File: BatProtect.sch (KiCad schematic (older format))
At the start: 57 parts, among them J1 PC104, J13 Charge3+, J16 uInv2+, J17 uInv1+, J19 uInv3+, J2 VBat1+, J3 BCharge1+, J4 BCharge3+, J5 Charge1+, J7 BCharge2+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

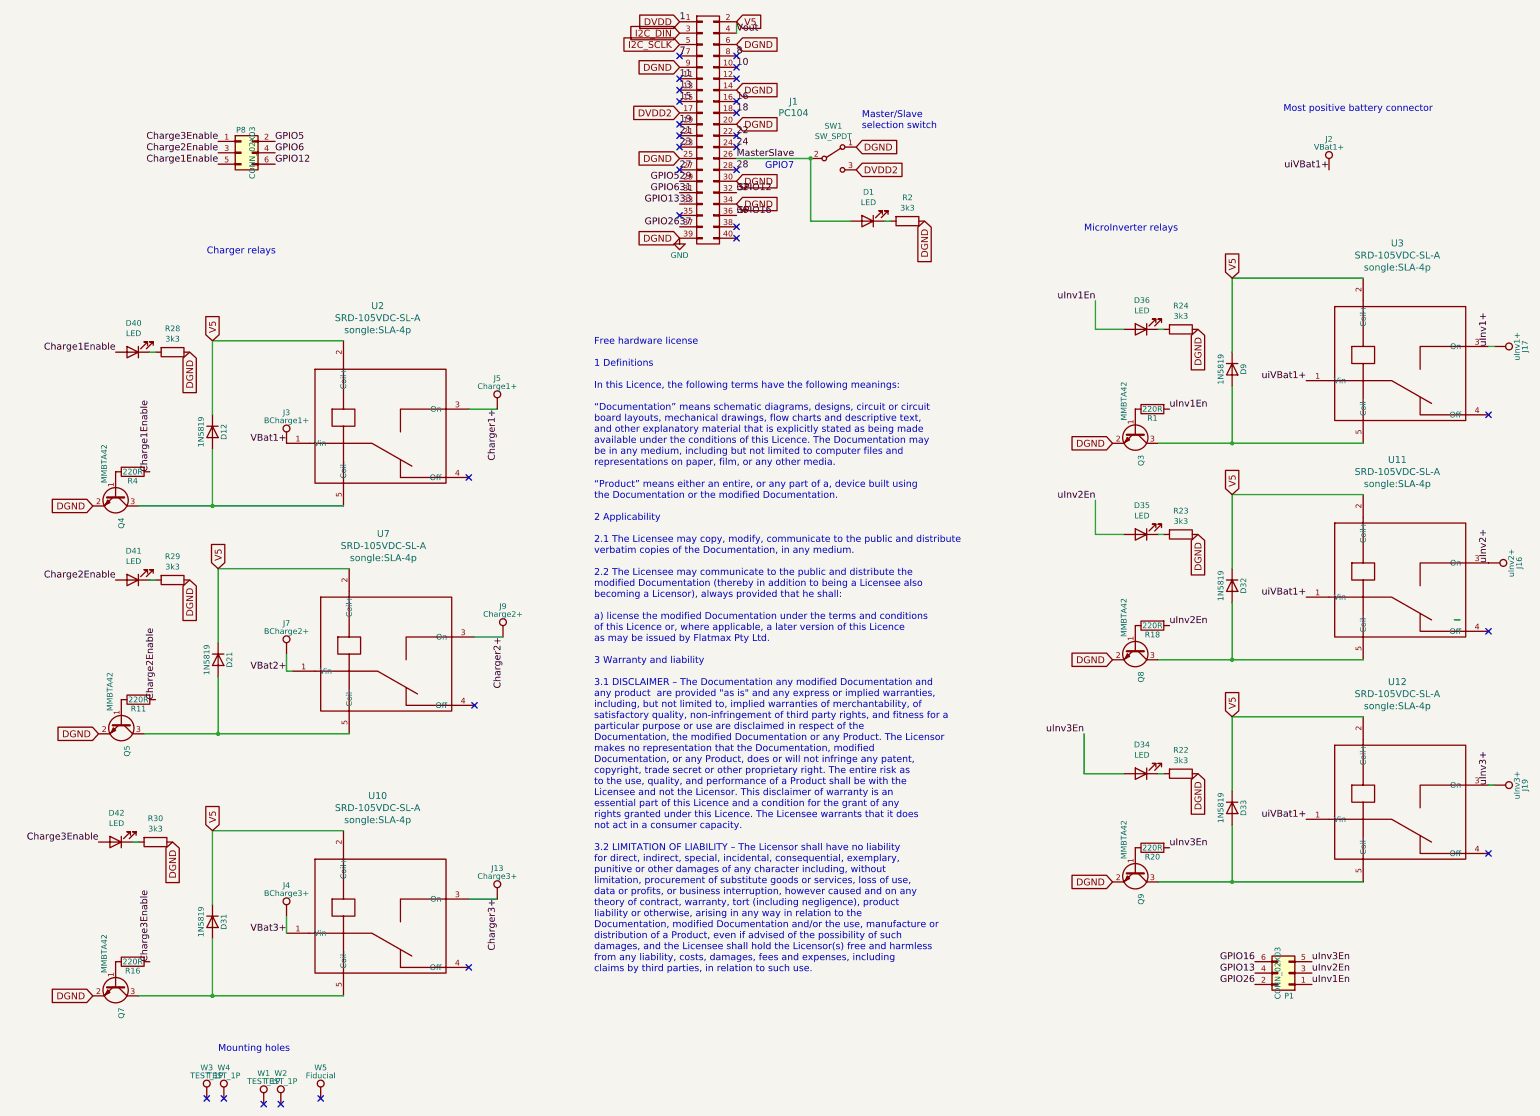
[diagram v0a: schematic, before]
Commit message: v2.0 Changed to AC mains relay switching.
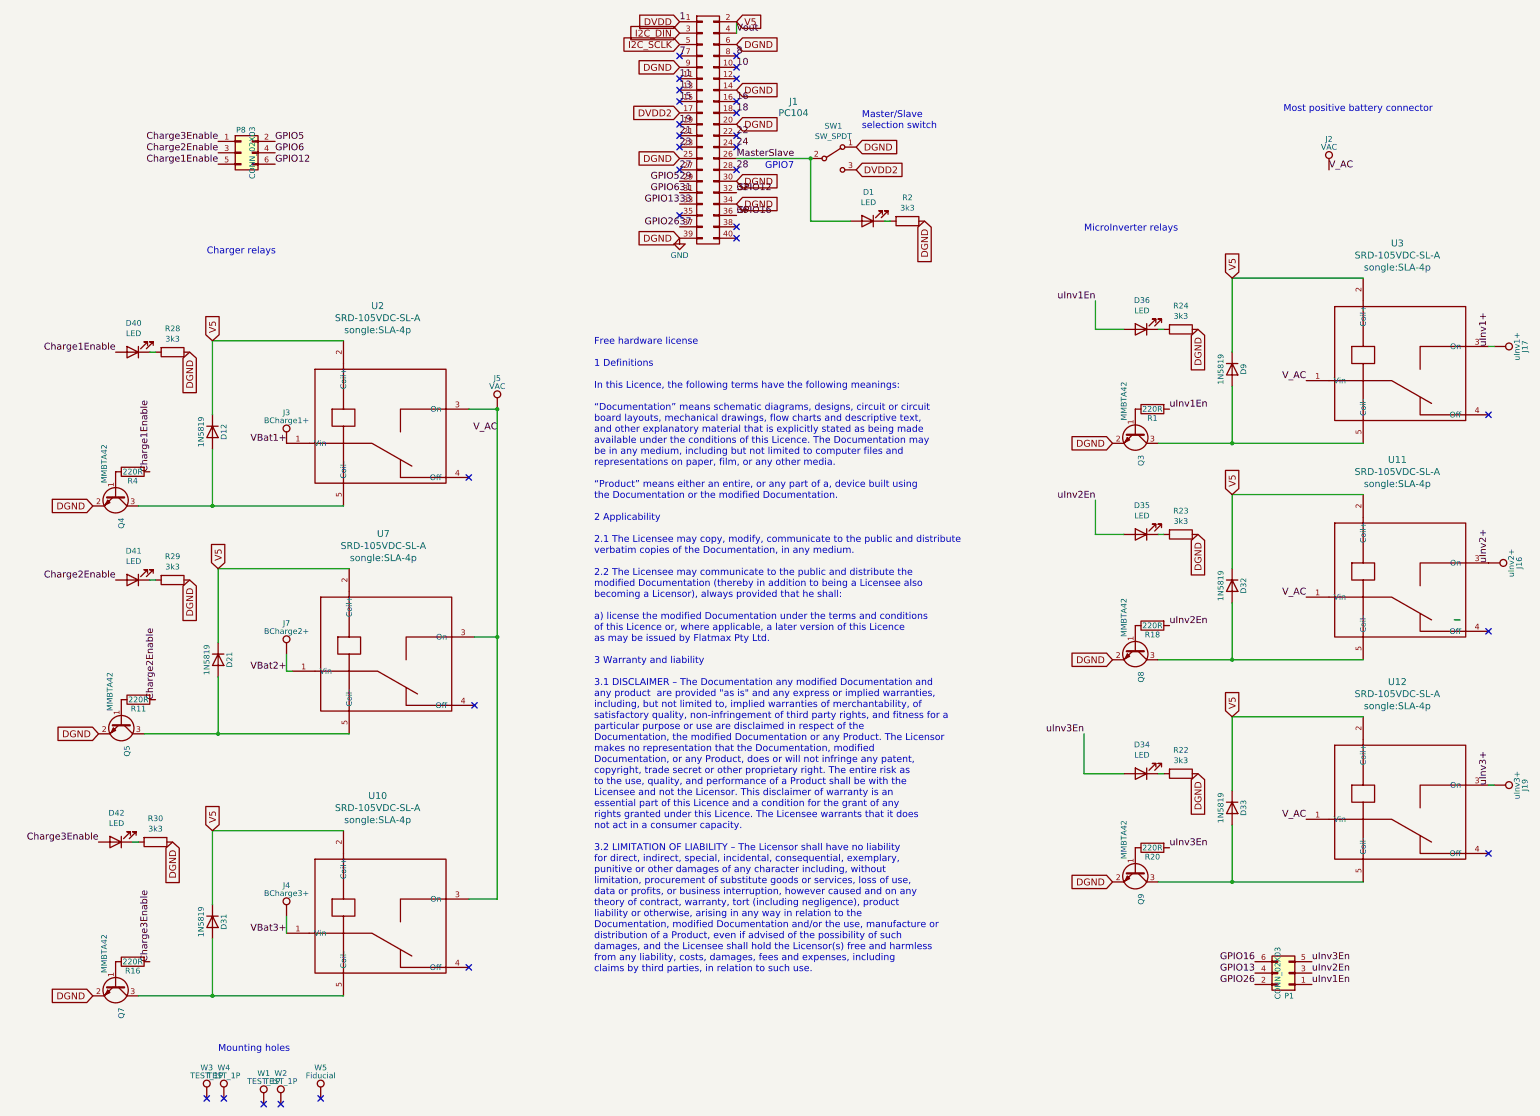
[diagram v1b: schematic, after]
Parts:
- removed J13: Charge3+, holes:Pin4mm, symbol BatProtect-rescue:TEST_1P
- removed J9: Charge2+, holes:Pin4mm, symbol BatProtect-rescue:TEST_1P
- J2: value VBat1+ -> VAC
- J5: value Charge1+ -> VAC
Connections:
- net labels added: V_AC
- net labels removed: Charger1+, Charger2+, Charger3+, uiVBat1+
- wire segments 56 -> 58
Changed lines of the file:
@@
 EESchema Schematic File Version 4
-LIBS:BatProtect-cache
 EELAYER 30 0
 EELAYER END
@@
 P 5850 4500
 F 0 "J5" H 5850 4770 50  0000 C CNN
-F 1 "Charge1+" H 5850 4700 50  0000 C CNN
+F 1 "VAC" H 5850 4700 50  0000 C CNN
 F 2 "holes:Pin4mm" H 6050 4500 50  0001 C CNN
 F 3 "" H 6050 4500 50  0000 C CNN
@@
 Text Label 2800 5050 1    60   ~ 0
 Charge1Enable
-Text Label 5850 4500 3    60   ~ 0
-Charger1+
 NoConn ~ 5600 5100
 $Comp
@@
 	1    0    0    -1
 $EndComp
-$Comp
-L BatProtect-rescue:TEST_1P J9
-U 1 1 5D644226
-P 5900 6500
-F 0 "J9" H 5900 6770 50  0000 C CNN
-F 1 "Charge2+" H 5900 6700 50  0000 C CNN
-F 2 "holes:Pin4mm" H 6100 6500 50  0001 C CNN
-F 3 "" H 6100 6500 50  0000 C CNN
-	1    5900 6500
-	1    0    0    -1
-$EndComp
 Text Label 2850 7050 1    60   ~ 0
 Charge2Enable
-Text Label 5900 6500 3    60   ~ 0
-Charger2+
 NoConn ~ 5650 7100
 $Comp
@@
 DGND
 Connection ~ 3400 7350
-Wire Wire Line
-	5650 6500 5900 6500
 $Comp
 L srd-12vdc-sl-c:SRD-12VDC-SL-C U7
@@
 	1    0    0    -1
 $EndComp
-$Comp
-L BatProtect-rescue:TEST_1P J13
-U 1 1 5D6503F2
-P 5850 8800
-F 0 "J13" H 5850 9070 50  0000 C CNN
-F 1 "Charge3+" H 5850 9000 50  0000 C CNN
-F 2 "holes:Pin4mm" H 6050 8800 50  0001 C CNN
-F 3 "" H 6050 8800 50  0000 C CNN
-	1    5850 8800
-	1    0    0    -1
-$EndComp
 Text Label 2800 9350 1    60   ~ 0
 Charge3Enable
-Text Label 5850 8800 3    60   ~ 0
-Charger3+
 NoConn ~ 5600 9400
 $Comp
@@
 P 13150 2400
 F 0 "J2" H 13150 2670 50  0000 C CNN
-F 1 "VBat1+" H 13150 2600 50  0000 C CNN
+F 1 "VAC" H 13150 2600 50  0000 C CNN
 F 2 "holes:Pin4mm" H 13350 2400 50  0001 C CNN
 F 3 "" H 13350 2400 50  0000 C CNN
@@
 	1    0    0    -1
 $EndComp
-Text Label 12950 4250 2    60   ~ 0
-uiVBat1+
 $Comp
 L BatProtect-rescue:TEST_1P J7
@@
 	1    0    0    -1
 $EndComp
-Text Label 12950 6150 2    60   ~ 0
-uiVBat1+
-Text Label 12950 8100 2    60   ~ 0
-uiVBat1+
 NoConn ~ 4300 10550
 Text Label 4000 4800 2    60   ~ 0
@@
 Text Label 4000 9100 2    60   ~ 0
 VBat3+
-Text Label 13150 2400 2    60   ~ 0
-uiVBat1+
 $Comp
 L BatProtect-rescue:TEST_1P J3
@@
 Text Notes 6700 9450 0    60   ~ 0
 Free hardware license\n\n1 Definitions\n\nIn this Licence, the following terms have the following meanings:\n\n“Documentation” means schematic diagrams, designs, circuit or circuit\nboard layouts, mechanical drawings, flow charts and descriptive text,\nand other explanatory material that is explicitly stated as being made\navailable under the conditions of this Licence. The Documentation may\nbe in any medium, including but not limited to computer files and\nrepresentations on paper, film, or any other media.\n\n“Product” means either an entire, or any part of a, device built using\nthe Documentation or the modified Documentation.\n\n2 Applicability\n\n2.1 The Licensee may copy, modify, communicate to the public and distribute\nverbatim copies of the Documentation, in any medium.\n\n2.2 The Licensee may communicate to the public and distribute the\nmodified Documentation (thereby in addition to being a Licensee also\nbecoming a Licensor), always provided that he shall:\n\na) license the modified Documentation under the terms and conditions\nof this Licence or, where applicable, a later version of this Licence\nas may be issued by Flatmax Pty Ltd.\n\n3 Warranty and liability\n\n3.1 DISCLAIMER – The Documentation any modified Documentation and\nany product  are provided "as is" and any express or implied warranties,\nincluding, but not limited to, implied warranties of merchantability, of\nsatisfactory quality, non-infringement of third party rights, and fitness for a\nparticular purpose or use are disclaimed in respect of the\nDocumentation, the modified Documentation or any Product. The Licensor\nmakes no representation that the Documentation, modified\nDocumentation, or any Product, does or will not infringe any patent,\ncopyright, trade secret or other proprietary right. The entire risk as\nto the use, quality, and performance of a Product shall be with the\nLicensee and not the Licensor. This disclaimer of warranty is an\nessential part of this Licence and a condition for the grant of any\nrights granted under this Licence. The Licensee warrants that it does\nnot act in a consumer capacity.\n\n3.2 LIMITATION OF LIABILITY – The Licensor shall have no liability\nfor direct, indirect, special, incidental, consequential, exemplary,\npunitive or other damages of any character including, without\nlimitation, procurement of substitute goods or services, loss of use,\ndata or profits, or business interruption, however caused and on any\ntheory of contract, warranty, tort (including negligence), product\nliability or otherwise, arising in any way in relation to the\nDocumentation, modified Documentation and/or the use, manufacture or\ndistribution of a Product, even if advised of the possibility of such\ndamages, and the Licensee shall hold the Licensor(s) free and harmless\nfrom any liability, costs, damages, fees and expenses, including\nclaims by third parties, in relation to such use.\n
+Wire Wire Line
+	5850 4500 5850 6500
+Connection ~ 5850 4500
+Wire Wire Line
+	5650 6500 5850 6500
+Connection ~ 5850 6500
+Wire Wire Line
+	5850 6500 5850 8800
+Text Label 13150 2400 0    60   ~ 0
+V_AC
+Text Label 12950 4250 2    60   ~ 0
+V_AC
+Text Label 12950 6150 2    60   ~ 0
+V_AC
+Text Label 12950 8100 2    60   ~ 0
+V_AC
+Text Label 5850 4700 2    60   ~ 0
+V_AC
 $EndSCHEMATC

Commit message: Switched relay names.
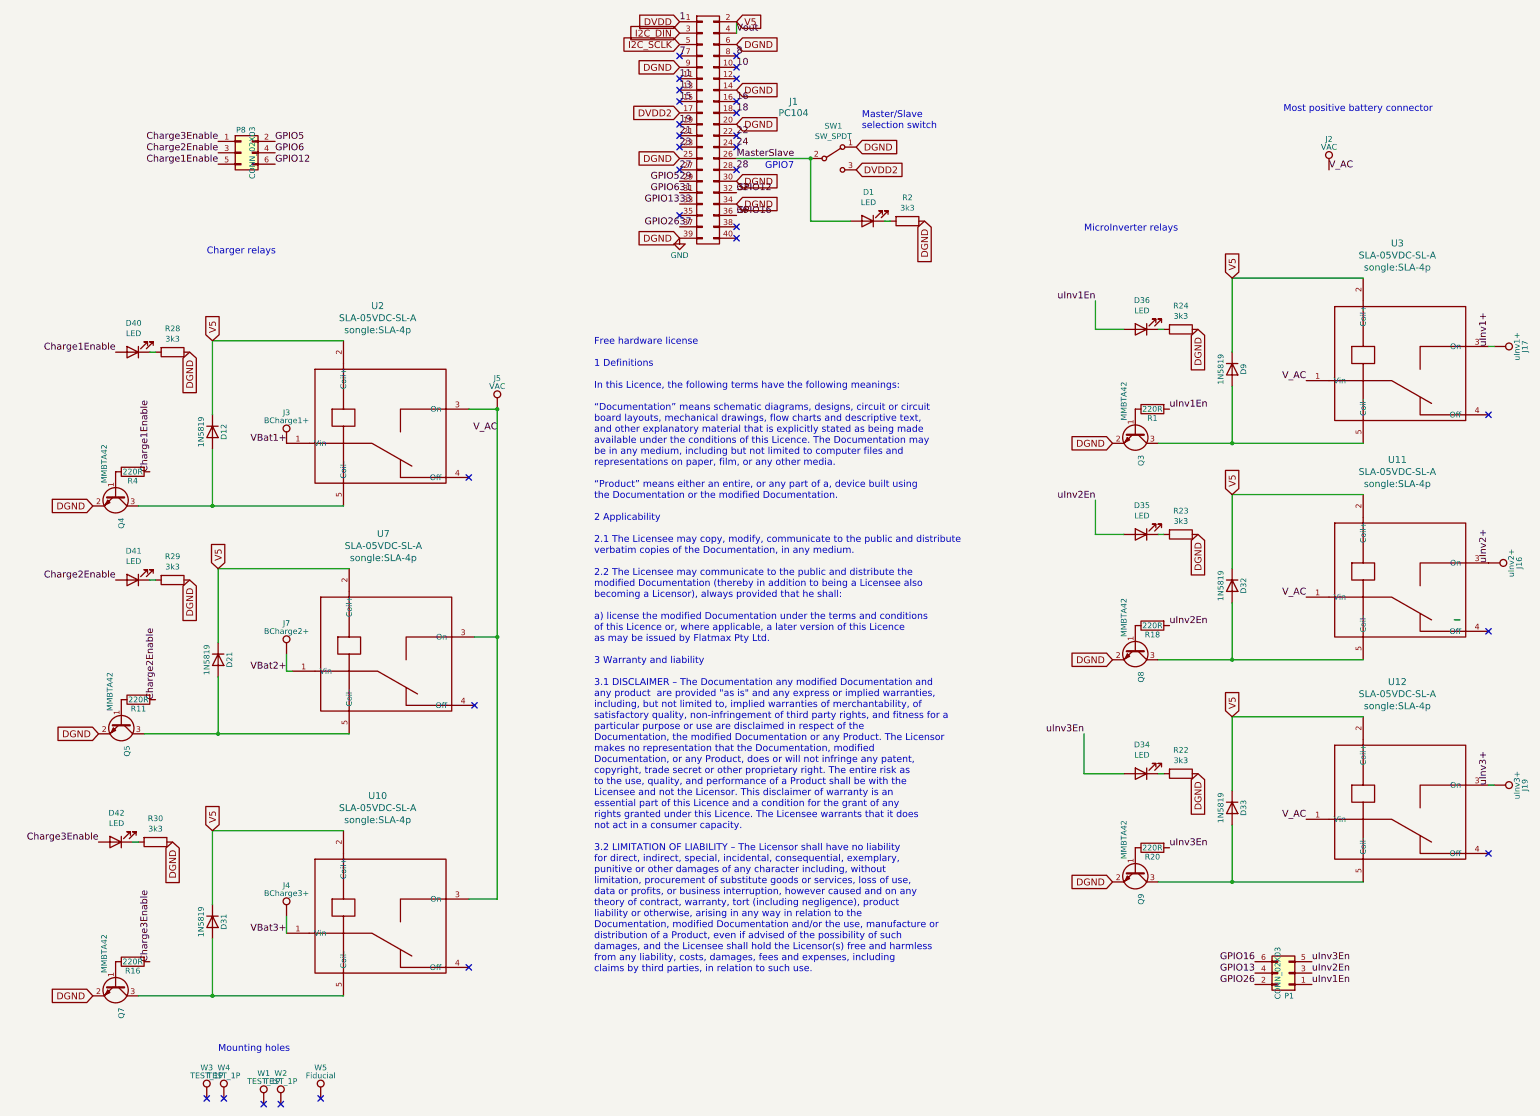
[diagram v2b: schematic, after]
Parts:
- U10, U11, U12, U2, U3, U7: value SRD-105VDC-SL-A -> SLA-05VDC-SL-A
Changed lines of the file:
@@
 Text Label 14550 3950 1    60   ~ 0
 uInv1+
-$Comp
-L srd-12vdc-sl-c:SRD-12VDC-SL-C U3
-U 1 1 5D6292DF
-P 13850 4250
-F 0 "U3" H 13750 5456 60  0000 C CNN
-F 1 "SRD-105VDC-SL-A" H 13750 5350 60  0000 C CNN
-F 2 "songle:SLA-4p" H 13750 5244 60  0000 C CNN
-F 3 "" H 13850 4250 60  0000 C CNN
-	1    13850 4250
-	1    0    0    -1
-$EndComp
 NoConn ~ 14550 4550
 $Comp
@@
 P 4900 4800
 F 0 "U2" H 4800 6006 60  0000 C CNN
-F 1 "SRD-105VDC-SL-A" H 4800 5900 60  0000 C CNN
+F 1 "SLA-05VDC-SL-A" H 4800 5900 60  0000 C CNN
 F 2 "songle:SLA-4p" H 4800 5794 60  0000 C CNN
 F 3 "" H 4900 4800 60  0000 C CNN
@@
 P 4950 6800
 F 0 "U7" H 4850 8006 60  0000 C CNN
-F 1 "SRD-105VDC-SL-A" H 4850 7900 60  0000 C CNN
+F 1 "SLA-05VDC-SL-A" H 4850 7900 60  0000 C CNN
 F 2 "songle:SLA-4p" H 4850 7794 60  0000 C CNN
 F 3 "" H 4950 6800 60  0000 C CNN
@@
 P 4900 9100
 F 0 "U10" H 4800 10306 60  0000 C CNN
-F 1 "SRD-105VDC-SL-A" H 4800 10200 60  0000 C CNN
+F 1 "SLA-05VDC-SL-A" H 4800 10200 60  0000 C CNN
 F 2 "songle:SLA-4p" H 4800 10094 60  0000 C CNN
 F 3 "" H 4900 9100 60  0000 C CNN
@@
 P 13850 6150
 F 0 "U11" H 13750 7356 60  0000 C CNN
-F 1 "SRD-105VDC-SL-A" H 13750 7250 60  0000 C CNN
+F 1 "SLA-05VDC-SL-A" H 13750 7250 60  0000 C CNN
 F 2 "songle:SLA-4p" H 13750 7144 60  0000 C CNN
 F 3 "" H 13850 6150 60  0000 C CNN
@@
 P 13850 8100
 F 0 "U12" H 13750 9306 60  0000 C CNN
-F 1 "SRD-105VDC-SL-A" H 13750 9200 60  0000 C CNN
+F 1 "SLA-05VDC-SL-A" H 13750 9200 60  0000 C CNN
 F 2 "songle:SLA-4p" H 13750 9094 60  0000 C CNN
 F 3 "" H 13850 8100 60  0000 C CNN
@@
 Text Label 5850 4700 2    60   ~ 0
 V_AC
+$Comp
+L srd-12vdc-sl-c:SRD-12VDC-SL-C U3
+U 1 1 5D6292DF
+P 13850 4250
+F 0 "U3" H 13750 5456 60  0000 C CNN
+F 1 "SLA-05VDC-SL-A" H 13750 5350 60  0000 C CNN
+F 2 "songle:SLA-4p" H 13750 5244 60  0000 C CNN
+F 3 "" H 13850 4250 60  0000 C CNN
+	1    13850 4250
+	1    0    0    -1
+$EndComp
 $EndSCHEMATC
